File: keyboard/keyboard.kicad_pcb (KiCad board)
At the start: 2 copper layers, 137 x 45.8 mm, 32 parts, among them SW10 KH-6X6X6H-STM, SW11 KH-6X6X6H-STM, SW12 KH-6X6X6H-STM, SW13 KH-6X6X6H-STM, SW14 KH-6X6X6H-STM, SW3 KH-6X6X6H-STM, SW4 KH-6X6X6H-STM, SW5 KH-6X6X6H-STM, SW6 KH-6X6X6H-STM, SW7 KH-6X6X6H-STM, SW8 KH-6X6X6H-STM, SW9 KH-6X6X6H-STM, U12 TM1638

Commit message: feat: 添加数码管键盘小板的铺铜
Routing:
- net /GND_IN: track 15.3 -> 17.7 mm, vias 1 -> 30
- net /SEG4: vias 5 -> 4
- added copper zone on B.Cu, net /GND_IN
- added copper zone on F.Cu, net /GND_IN

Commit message: update: 添加按键小板电源指示灯并优化布线
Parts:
- added D1: LED, LED_SMD:LED_0603_1608Metric, F.Cu at (150.8, 109.8)
- added R14: 4.7k, Resistor_SMD:R_0603_1608Metric, F.Cu at (150.8, 107.6)
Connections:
- net /5V_IN renamed /+5V
- net /GND_IN renamed /GND
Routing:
- net /+5V: track 53.1 -> 86.7 mm, vias 3 -> 4
- net Net-(D1-K): track 0.00 -> 4.92 mm, vias 0 -> 2
- net Net-(D3-K): track 20.3 -> 19.4 mm
- net /GND: vias 30 -> 34
- net (no net): vias 0 -> 1

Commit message: update: 添加键盘签名
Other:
- board text added: "Designed by Eazybot"
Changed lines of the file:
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@@
 		(tags "capacitor electrolytic")
 		(property "Reference" "C22"
-			(at -6.5 0 180)
+			(at 4.4 -2.4 180)
 			(layer "F.SilkS")
 			(effects
@@
 		(layer "Margin")
 	)
+	(gr_text "Designed by Eazybot"
+		(at 165.2 109.8 0)
+		(layer "B.SilkS")
+		(effects
+			(font
+				(size 1.5 1.5)
+				(thickness 0.3)
+				(bold yes)
+			)
+			(justify left bottom mirror)
+		)
+	)
 	(via

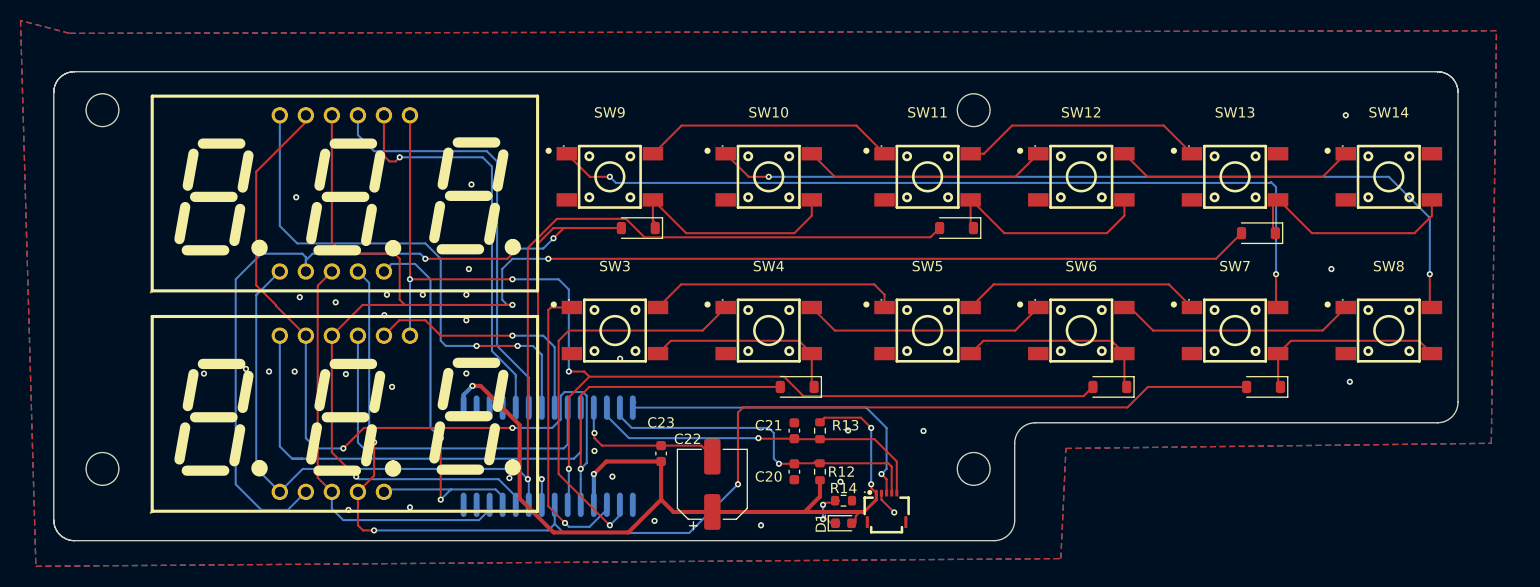
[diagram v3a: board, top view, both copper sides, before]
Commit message: update: 更新按钮小板设计，导出gerber文件
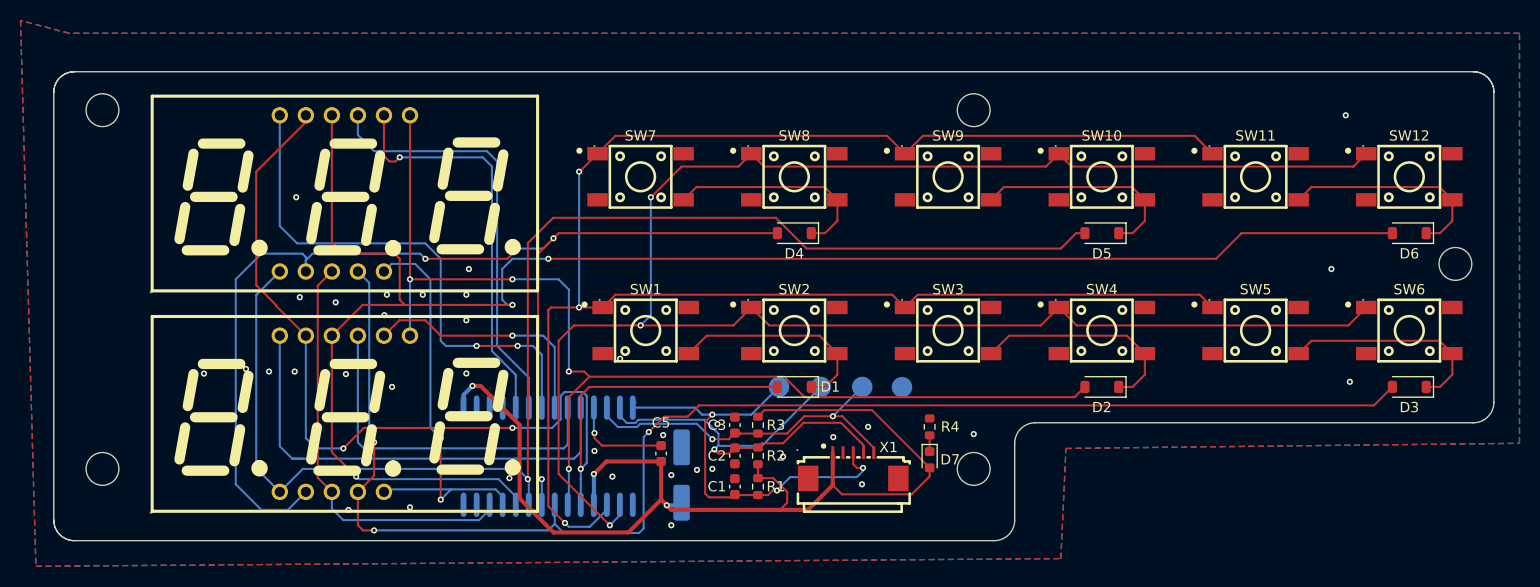
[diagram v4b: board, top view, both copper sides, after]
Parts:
- removed the D7 at (161.8, 81.0)
- removed D8: 1N4148W, Diode_SMD:D_SOD-123
- removed FPC1: HC-FPC-05-10-5RLTAG, lcsc_footprints:C5213728_FPC-SMD_5P-P0_50_HCTL_HC-FPC-05-10-5RLTAG
- removed R12, R13: 10k, Resistor_SMD:R_0603_1608Metric
- removed R14: 4.7k, Resistor_SMD:R_0603_1608Metric
- removed REF** (x4): MountingHole_3.2mm_M3, MountingHole:MountingHole_3.2mm_M3
- added ?: , , F.Cu at (78.5, 104.5)
- added ?: , , F.Cu at (163.5, 69.5)
- added ?: , , F.Cu at (210.5, 84.5)
- added ?: , , F.Cu at (163.5, 104.5)
- added ?: , , F.Cu at (78.5, 69.5)
- added C1: 100pF, Capacitor_SMD:C_0603_1608Metric, F.Cu at (140.2, 106.2)
- added D1: 1N4148W, Diode_SMD:D_SOD-123, F.Cu at (146.0, 96.5)
- added D2: 1N4148W, Diode_SMD:D_SOD-123, F.Cu at (176.0, 96.5)
- added R1: 10k, Resistor_SMD:R_0603_1608Metric, F.Cu at (142.4, 106.2)
- added R2: 10k, Resistor_SMD:R_0603_1608Metric, F.Cu at (142.4, 103.2)
- added R3: 10k, Resistor_SMD:R_0603_1608Metric, F.Cu at (142.4, 100.2)
- added R4: 4.7k, Resistor_SMD:R_0603_1608Metric, F.Cu at (159.2, 100.4)
- added TP1: TestPoint, TestPoint:TestPoint_Pad_D2.0mm, B.Cu at (144.5, 96.5)
- added TP2: TestPoint, TestPoint:TestPoint_Pad_D2.0mm, B.Cu at (148.6, 96.5)
- added TP3: TestPoint, TestPoint:TestPoint_Pad_D2.0mm, B.Cu at (152.6, 96.5)
- added TP4: TestPoint, TestPoint:TestPoint_Pad_D2.0mm, B.Cu at (156.5, 96.5)
- added X1: AFA01-S05FCA-00, lcsc_footprints:C262753_FPC-SMD_AFA01-S05FCA-00, F.Cu at (151.8, 104.2)
- C4: renamed from C22; moved to B.Cu
- moved D6 75.2 mm to (206.0, 81.5)
- moved D3 59.7 mm to (206.0, 96.5)
- moved D4 34.2 mm to (146.0, 81.5)
- moved D5 21.8 mm to (176.0, 81.5)
- moved D7 10.4 mm to (159.2, 103.6), turned to -90 degrees
- moved C2 6.00 mm to (140.2, 103.2)
- moved C3 5.83 mm to (140.2, 100.2)
- moved C4 3.13 mm to (135.0, 105.1)
- moved SW1 3.00 mm to (131.5, 91.0)
- moved SW7 3.00 mm to (131.0, 76.0)
- moved SW2 2.50 mm to (146.0, 91.0)
- moved SW8 2.50 mm to (146.0, 76.0)
- moved SW10 2.00 mm to (176.0, 76.0)
- moved SW11 2.00 mm to (191.0, 76.0)
- moved SW12 2.00 mm to (206.0, 76.0)
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- renumbered C20 to C2, C21 to C3, C23 to C5, D1 to D7, SW3 to SW1, SW12 to SW10, SW13 to SW11, SW14 to SW12, SW4 to SW2, SW5 to SW3, SW6 to SW4, SW7 to SW5, SW8 to SW6, SW9 to SW7, SW10 to SW8, SW11 to SW9, U12 to U1
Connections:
- net /+5V renamed +5V
- net /GND renamed GND
- D3 pad 2: /SEG1 -> /SEG3
- D4 pad 2: /SEG2 -> /SEG4
- D5 pad 2: /SEG3 -> /SEG5
- D6 pad 2: /SEG4 -> /SEG6
- SW1 pad 1: Net-(SW3-A) -> Net-(SW1-A)
- SW1 pad 2: Net-(SW3-B) -> unconnected-(SW1-B-Pad2)
- SW1 pad 4: Net-(D3-K) -> Net-(D1-K)
- SW10 pad 1: Net-(SW10-B) -> Net-(SW10-A)
- SW10 pad 2: Net-(SW12-B) -> unconnected-(SW10-B-Pad2)
- SW10 pad 4: Net-(D7-K) (its old number) -> Net-(D5-K)
- SW11 pad 1: Net-(SW11-B) -> Net-(SW1-A)
- SW11 pad 4: Net-(D8-K) -> Net-(D6-K)
- SW12 pad 1: Net-(SW12-B) -> Net-(SW10-A)
- SW12 pad 4: Net-(D8-K) -> Net-(D6-K)
- SW2 pad 1: Net-(SW4-A) -> Net-(SW10-A)
- SW2 pad 2: Net-(SW4-B) -> unconnected-(SW2-B-Pad2)
- SW2 pad 4: Net-(D3-K) -> Net-(D1-K)
- SW3 pad 1: Net-(SW3-B) -> Net-(SW1-A)
- SW3 pad 2: Net-(SW5-B) -> unconnected-(SW3-B-Pad2)
- SW3 pad 4: Net-(D4-K) -> Net-(D2-K)
- SW4 pad 1: Net-(SW4-B) -> Net-(SW10-A)
- SW4 pad 2: Net-(SW6-B) -> unconnected-(SW4-B-Pad2)
- SW4 pad 4: Net-(D4-K) -> Net-(D2-K)
- SW5 pad 1: Net-(SW5-B) -> Net-(SW1-A)
- SW5 pad 2: Net-(SW7-B) -> unconnected-(SW5-B-Pad2)
- SW5 pad 4: Net-(D5-K) -> Net-(D3-K)
- SW6 pad 1: Net-(SW6-B) -> Net-(SW10-A)
- SW6 pad 2: Net-(SW10-A) -> unconnected-(SW6-B-Pad2)
- SW6 pad 4: Net-(D5-K) -> Net-(D3-K)
- SW7 pad 1: Net-(SW7-B) -> Net-(SW1-A)
- SW7 pad 2: Net-(SW11-A) -> unconnected-(SW7-B-Pad2)
- SW7 pad 4: Net-(D6-K) -> Net-(D4-K)
- SW8 pad 2: Net-(SW10-B) -> unconnected-(SW8-B-Pad2)
- SW8 pad 4: Net-(D6-K) -> Net-(D4-K)
- SW9 pad 1: Net-(SW11-A) -> Net-(SW1-A)
- SW9 pad 2: Net-(SW11-B) -> unconnected-(SW9-B-Pad2)
- SW9 pad 4: Net-(D7-K) (its old number) -> Net-(D5-K)
- U1 pad 2: Net-(SW4-A) -> Net-(SW10-A)
- U1 pad 3: Net-(SW3-A) -> Net-(SW1-A)
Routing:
- net Net-(SW1-A): track 0.00 -> 172.5 mm, vias 0 -> 3
- net Net-(SW10-A): track 80.1 -> 192.1 mm, vias 2 -> 3
- net Net-(SW7-B): track 82.5 -> 0.00 mm, vias 2 -> 0
- net Net-(SW4-A): track 40.1 -> 0.00 mm, vias 1 -> 0
- net Net-(SW3-A): track 29.3 -> 0.00 mm, vias 1 -> 0
- net Net-(SW11-A): track 24.9 -> 0.00 mm
- net Net-(SW3-B): track 24.7 -> 0.00 mm
- net Net-(SW4-B): track 24.0 -> 0.00 mm
- net Net-(SW10-B): track 24.0 -> 0.00 mm
- net Net-(SW11-B): track 23.9 -> 0.00 mm
- net Net-(SW12-B): track 23.5 -> 0.00 mm
- net Net-(SW6-B): track 23.5 -> 0.00 mm
- net Net-(SW5-B): track 23.5 -> 0.00 mm
- net Net-(D2-K): track 0.00 -> 21.5 mm
- net Net-(D7-K) (its old number): track 21.5 -> 0.00 mm
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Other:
- board size 137 x 45.8 mm -> 140.5 x 45.8 mm
- board text added: "CLK"
- board text added: "DIO"
- board text added: "Designed by Eazybot & 布谷鸟"
- board text added: "GND"
- board text added: "STB"
- board text removed: "Designed by Eazybot"
